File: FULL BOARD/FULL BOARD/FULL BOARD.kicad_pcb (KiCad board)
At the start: 2 copper layers, 200 x 200 mm, 100 parts, among them IC1 TAS5760LDAP, J1 PJ-036AH-SMT-TR, J2 Micro_SD_Card, J3 B2B-PH-K-S, J4 5019514000, J5 61201021621, J6 B2B-PH-K-S, SW1 SW_Push, U1 LD1117S33TR_SOT223, U2 STM32H743VITx, Y1 ABLS7M2-16.000MHZ-D-2Y-T

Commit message: Made some changes, not all made
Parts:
- C10, C11, C12, C13, C14, C16, C17, C18, C19, C2, C20, C21, C22, C23, C24, C25, C26, C27, C28, C29, C30, C31, C33, C5, C6, C7, C8, C9: footprint Capacitor_SMD:C_0402_1005Metric -> Capacitor_SMD:C_0805_2012Metric
- C3: footprint Capacitor_SMD:C_0603_1608Metric -> Capacitor_SMD:C_0805_2012Metric
- J3, J6: moved to B.Cu
- moved J3 2.02 mm to (86.7, 173.5), turned to 180 degrees
- moved J6 2.00 mm to (248.7, 173.5), turned to 180 degrees
- moved J1 1.71 mm to (83.0, 51.4)
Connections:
- C24 pad 2: GND -> +3.3V
- IC1 pad 33: +5V -> GND
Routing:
- net +5V: track 380.5 -> 334.1 mm
- net Net-(IC1-SPK_OUTB+): track 230.0 -> 199.6 mm, vias 1 -> 0
- net Net-(IC1-SPK_OUTB-): track 217.8 -> 195.8 mm, vias 1 -> 0
- net Net-(IC1-SPK_OUTA+): track 54.1 -> 40.6 mm
- net Net-(IC1-SPK_OUTA-): track 57.0 -> 44.5 mm
- net GND: track 266.7 -> 259.2 mm

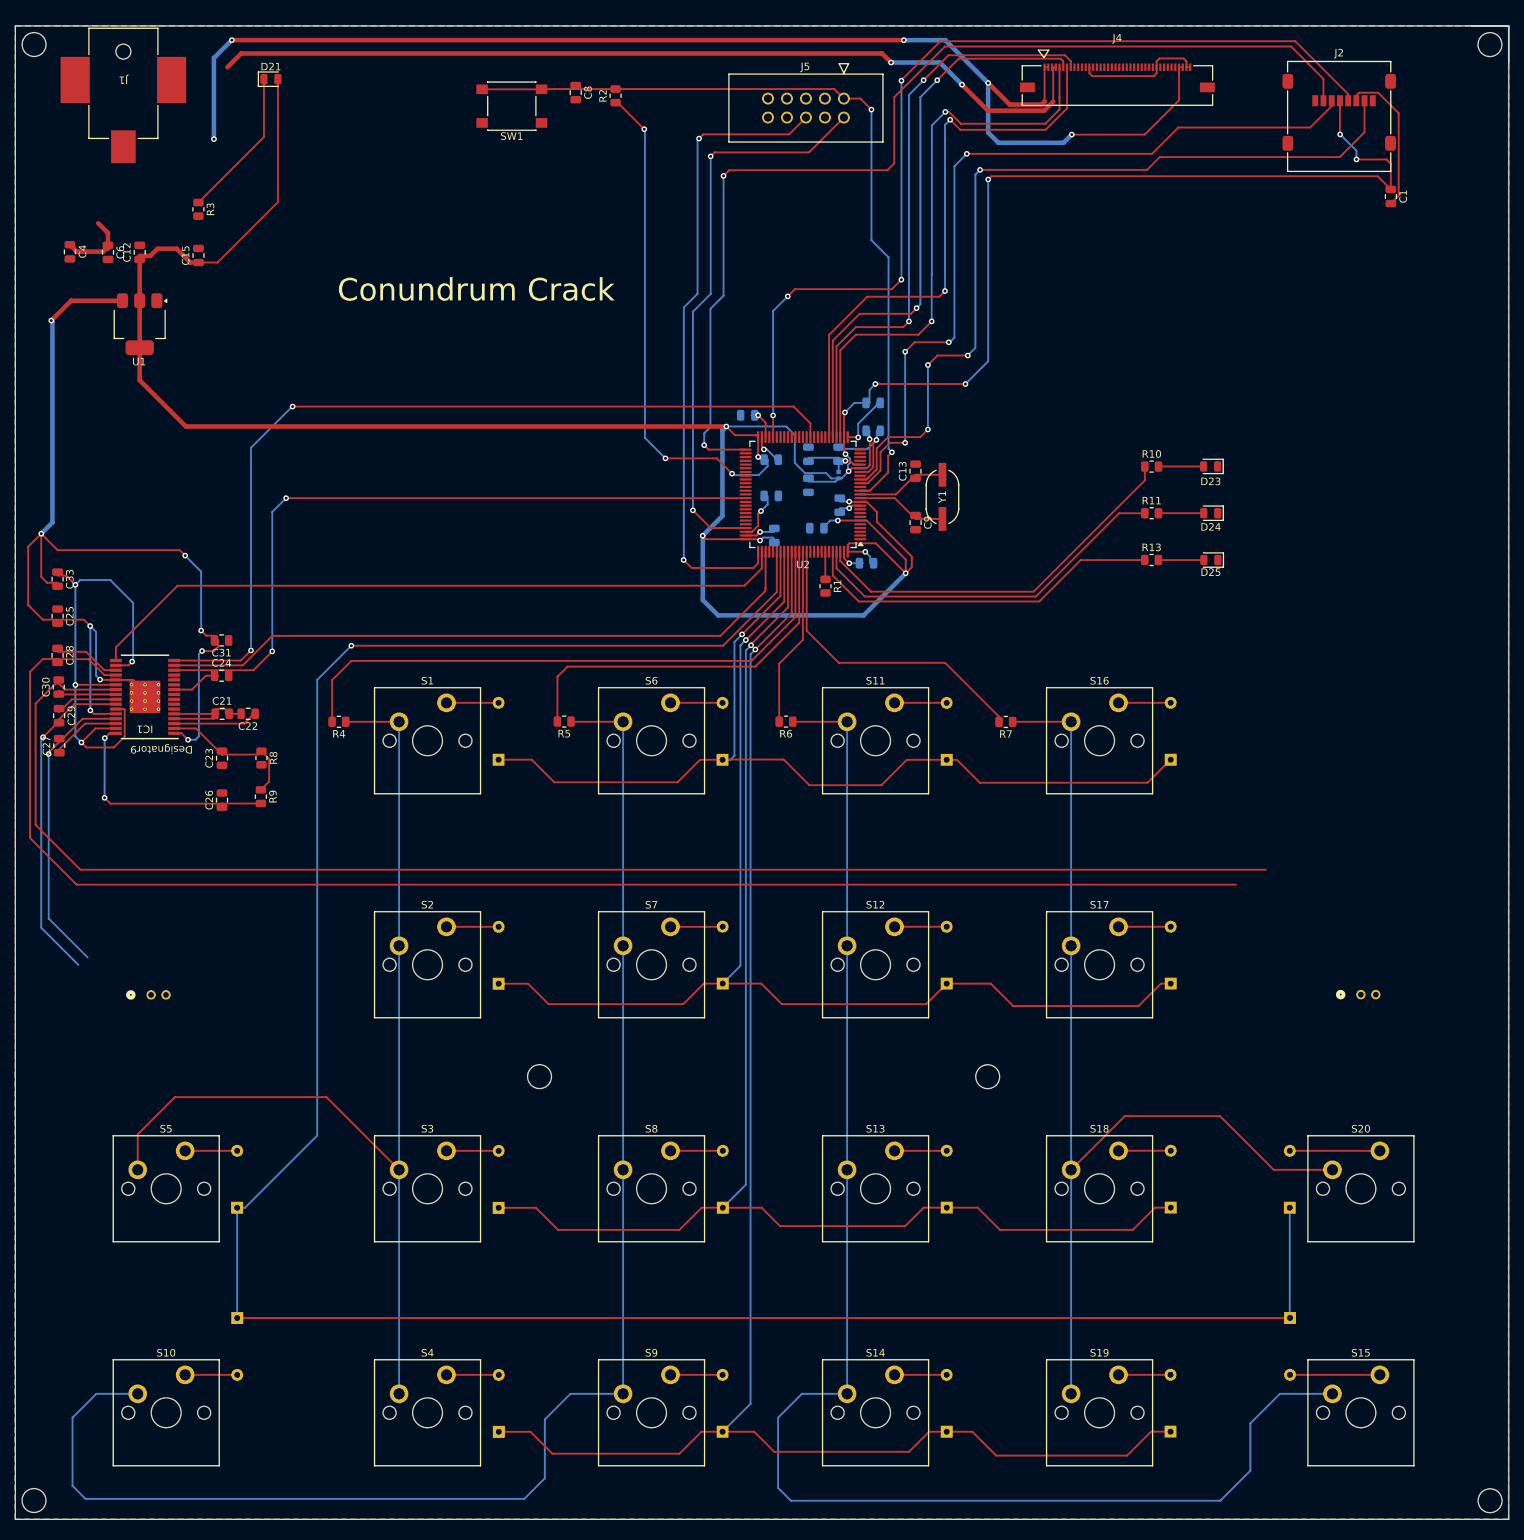
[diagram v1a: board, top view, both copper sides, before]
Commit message: Updated micro routing, not finished
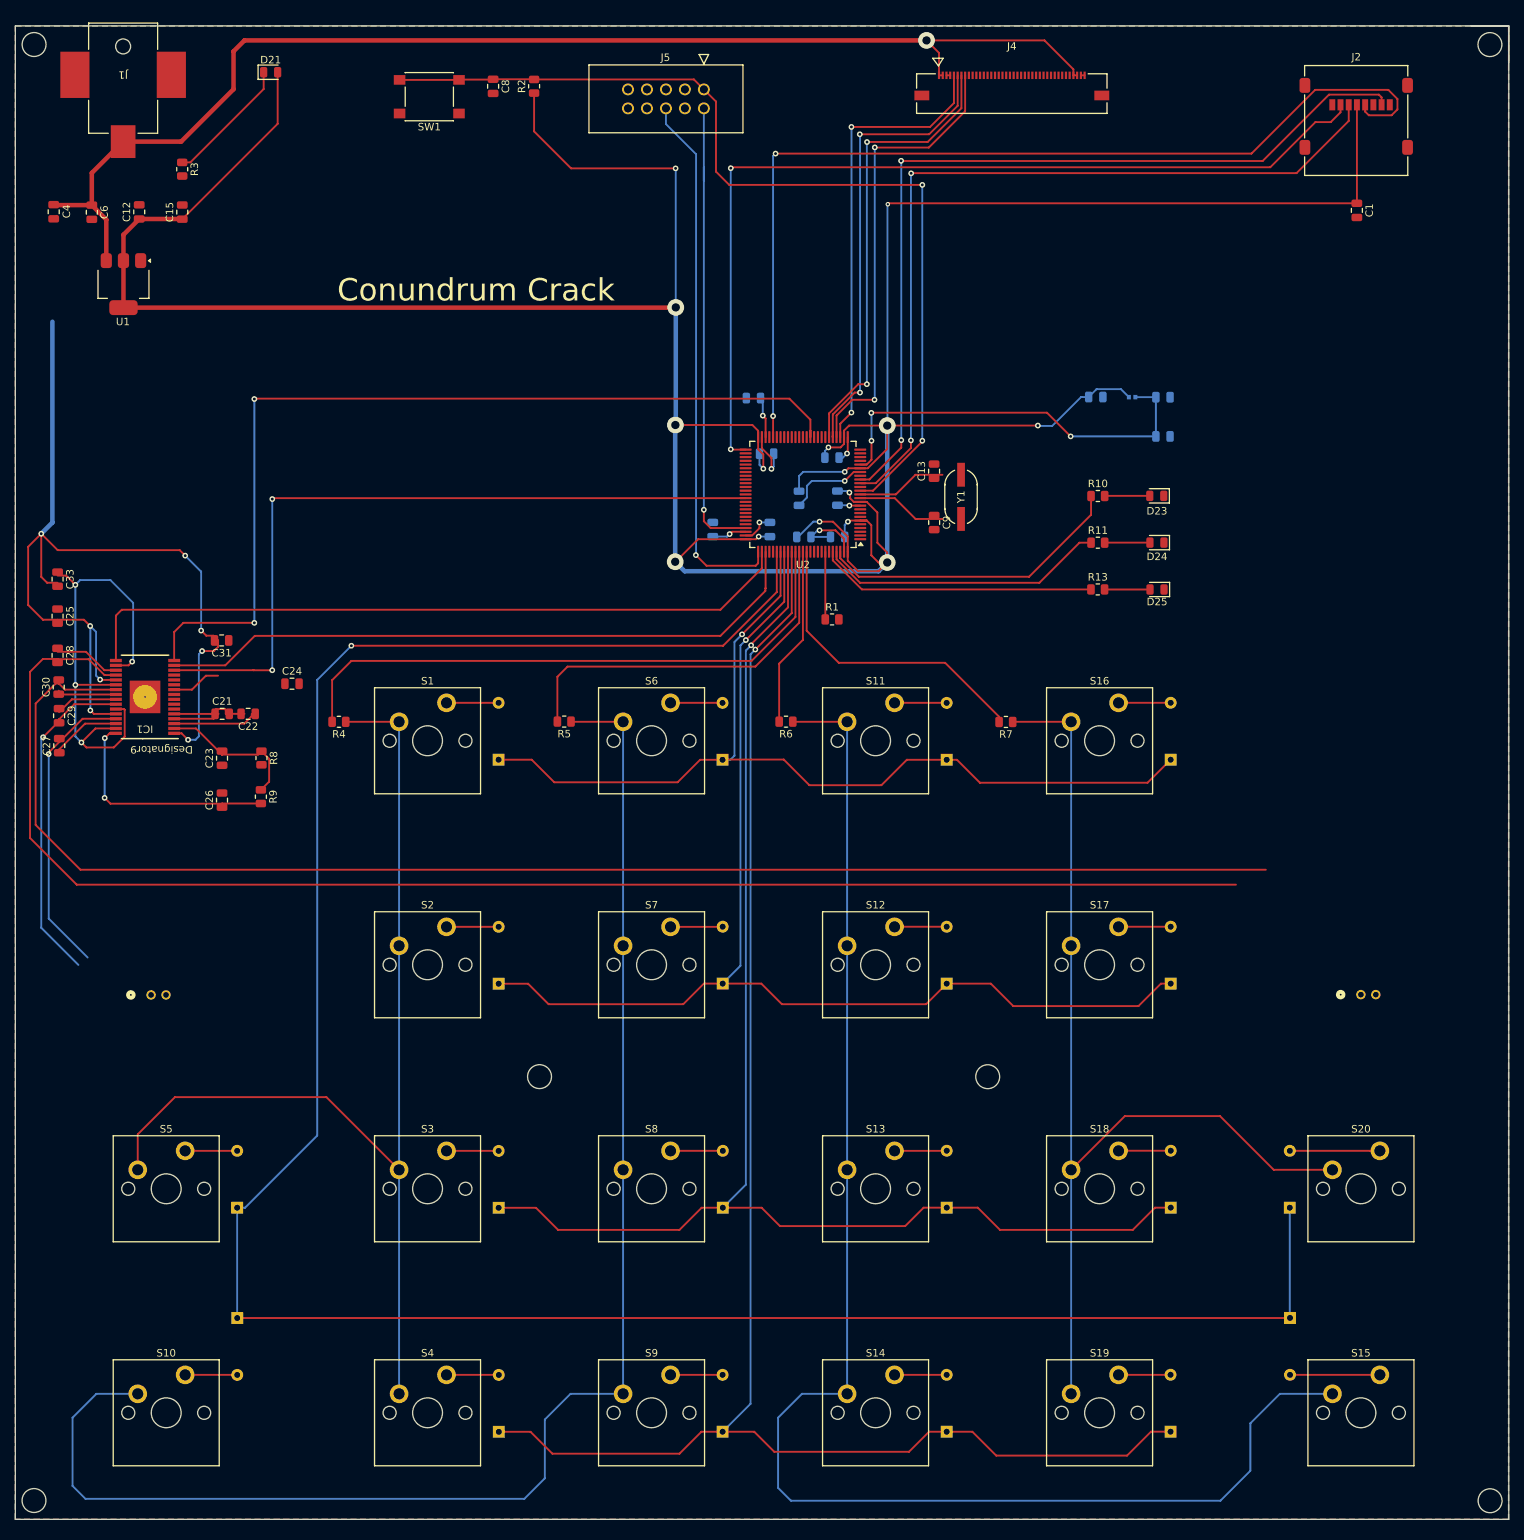
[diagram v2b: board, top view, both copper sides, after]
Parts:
- moved C18 47.5 mm to (222.2, 98.7), turned to 0 degrees
- moved C19 44.1 mm to (222.2, 93.5), turned to 0 degrees
- moved FL1 40.7 mm to (218.1, 93.5), turned to 180 degrees
- moved C20 30.2 mm to (213.2, 93.5)
- moved J5 18.8 mm to (160.8, 52.3)
- moved C5 16.2 mm to (173.5, 107.0), turned to -90 degrees
- moved J4 14.2 mm to (202.0, 52.8)
- moved SW1 11.1 mm to (124.0, 53.2)
- moved C8 11.1 mm to (132.5, 51.9)
- moved R2 11.0 mm to (138.0, 51.8)
- moved C11 9.55 mm to (178.7, 107.0), turned to -90 degrees
- moved C24 9.48 mm to (105.6, 131.9)
- moved C7 9.03 mm to (161.9, 111.2), turned to -90 degrees
- moved D24 8.21 mm to (221.4, 113.0)
- moved D25 8.21 mm to (221.4, 119.2)
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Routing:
- net GND: track 259.2 -> 107.4 mm, vias 12 -> 10
- net +3.3VA: track 9.22 -> 55.5 mm, vias 1 -> 3
- net +5V: track 334.1 -> 305.2 mm, vias 14 -> 9
- net /NRST: track 109.0 -> 126.3 mm
- net /LCD_SCK: track 78.6 -> 61.6 mm
- net /LCD_MOSI: track 77.8 -> 61.2 mm
- net /LCD_CS: track 76.7 -> 60.9 mm
- net /LCD_MISO: track 76.6 -> 61.4 mm
- net /SD_CS: track 140.4 -> 125.4 mm
- net /SWDIO: track 76.4 -> 63.1 mm, vias 2 -> 1
- net /SWC: track 85.0 -> 72.1 mm, vias 2 -> 1
- net Net-(U2-PB9): track 48.7 -> 37.3 mm
- net Net-(U2-PE0): track 49.7 -> 38.6 mm
- net Net-(U2-PE1): track 51.7 -> 41.4 mm
- net +3.3V: track 485.4 -> 493.3 mm, vias 20 -> 15
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
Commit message: Rerouted board
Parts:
- C27, C28, C29, C30: moved to B.Cu
- moved C24 9.39 mm to (96.2, 132.6), turned to 90 degrees
- moved C27 8.57 mm to (73.4, 148.7)
- moved C29 8.57 mm to (73.4, 144.6)
- moved C30 8.57 mm to (73.3, 140.8)
- moved C25 8.57 mm to (73.2, 131.3), turned to 0 degrees
- moved C28 8.32 mm to (73.3, 136.3)
- moved C33 8.26 mm to (73.2, 126.0), turned to 0 degrees
- moved C22 2.38 mm to (101.5, 137.5), turned to -90 degrees
- moved C21 1.62 mm to (96.2, 137.5), turned to 90 degrees
- moved C13 1.06 mm to (190.5, 103.4)
- moved C9 1.02 mm to (190.6, 110.3)
- moved R9 0.52 mm to (101.5, 147.5)
- moved C23 0.52 mm to (96.2, 142.3)
- moved R8 0.52 mm to (101.5, 142.3)
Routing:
- net +3.3V: track 493.3 -> 588.0 mm, vias 15 -> 18
- net Net-(IC1-SPK_OUTB-): track 195.8 -> 235.5 mm, vias 0 -> 3
- net Net-(IC1-SPK_OUTB+): track 199.6 -> 237.7 mm, vias 0 -> 3
- net GND: track 107.4 -> 141.8 mm, vias 10 -> 11
- net Net-(IC1-SPK_OUTA-): track 44.5 -> 63.8 mm
- net Net-(IC1-SPK_OUTA+): track 40.6 -> 57.0 mm
- net +5V: track 305.2 -> 292.3 mm, vias 9 -> 5
- net /SD_CLK: track 132.6 -> 121.8 mm
- net Net-(IC1-BSTRPA+): track 9.12 -> 18.9 mm, vias 0 -> 1
- net Net-(IC1-BSTRPA-): track 8.43 -> 16.3 mm, vias 0 -> 1
- net Net-(IC1-BSTRPB-): track 7.99 -> 13.6 mm, vias 0 -> 1
- net Net-(IC1-ANA_REG): track 11.2 -> 16.5 mm
- net Net-(IC1-GVDD_REG): track 31.1 -> 26.6 mm, vias 2 -> 0
- net /SD_DO: track 114.9 -> 118.8 mm
- net /HSE_IN: track 12.2 -> 14.7 mm
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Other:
- outline, holes or cut-outs redrawn
